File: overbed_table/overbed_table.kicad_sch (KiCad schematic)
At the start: 0 parts

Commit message: 更新原理图
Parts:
- added C33, C42, C43, C44: 1uF, PCM_SparkFun-Resistor:R_0603_1608Metric, symbol Device:C
- added CN3: KF2EDGRC-5.08-2P, lcsc_footprints:C441236_CONN-TH_P5_08_KF2EDGRC-5_08-2P, symbol lcsc_imported:KF2EDGRC-5_08-2P
- added CN4: KF2EDGRC-5.08-4P, lcsc_footprints:C441238_CONN-TH_4P-P5_08_KF2EDGRC-5_08-4P, symbol lcsc_imported:KF2EDGRC-5_08-4P
- added D7: PMEG2010ER, Diode_SMD:Nexperia_CFP3_SOD-123W, symbol Diode:PMEG2010ER
- added H1: LAIL-PZ2.54-4P-L, lcsc_footprints:C54950602_CONN-TH_LAIL-PZ2_54-4P-L, symbol lcsc_imported:LAIL-PZ2_54-4P-L
- added R34, R37, R38, R44: 10k, PCM_SparkFun-Resistor:R_0603_1608Metric, symbol PCM_SparkFun-Resistor:R
- added R35, R36: 33, PCM_SparkFun-Resistor:R_0603_1608Metric, symbol PCM_SparkFun-Resistor:R
- added SW13, SW14: KH-6X6X6H-STM, lcsc_footprints:C2837532_SW-SMD_4P-L6_0-W6_0-P4_50-LS9_0_KH-6X6X6H-STM, symbol lcsc_imported:KH-6X6X6H-STM
- added TP11: TestPoint, symbol Connector:TestPoint
- added U13, U15, U18: WAFER-XH254WZ-2A, lcsc_footprints:C7432691_CONN-TH_2P-P2_50_WAFER-XH254WZ-2A, symbol lcsc_imported:WAFER-XH254WZ-2A
- added U19: AP2112K-3.3TRG1, lcsc_footprints:C51118_SOT-25-5_L2_9-W1_6-P0_95-LS2_8-BL, symbol lcsc_imported:AP2112K-3_3TRG1
- added U6: ESP32-C3-WROOM-02, RF_Module:ESP32-C3-WROOM-02, symbol RF_Module:ESP32-C3-WROOM-02
- added X1, X2: AFA01-S05FCA-00, lcsc_footprints:C262753_FPC-SMD_AFA01-S05FCA-00, symbol lcsc_imported:AFA01-S05FCA-00
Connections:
- net 12V_5V/5V_OUT: now also X2.4
- net GND: now also C33.2, C42.2, C43.1, C44.2, CN3.1, CN4.4, H1.4, R44.2, SW13.4 (D), SW14.4 (D), U19.2 (GND), U6.19 (GND), U6.9 (GND), X2.5, X2.6, X2.7
- net 数码管_按钮/5V_IN: now also X1.4
- net 数码管_按钮/CLK: now also X1.2
- net 数码管_按钮/DIO: now also X1.3
- net 数码管_按钮/GND_IN: now also X1.5, X1.6, X1.7
- net 数码管_按钮/STB: now also X1.1
- new net: C43.2, H1.1, U19.1 (VIN), U19.3 (EN)
- new net: R35.1, U6.13 (IO18)
- new net: R36.1, U6.14 (IO19)
- new net: TP11.1, U6.6 (IO7)
- new net: C44.1, D7.2 (A), U19.5 (VOUT)
- new net +12V: CN3.2, CN4.3, U13.1, U15.1
- new net +3V3: D7.1 (K), R34.1, R37.1, R38.1, U18.1, U6.1 (3V3)
- new net 3V3_5V_转换器/3V3_SIG0: X2.3
- new net 3V3_5V_转换器/3V3_SIG1: X2.2
- new net 3V3_5V_转换器/3V3_SIG2: X2.1
- new net 3V3_5V_转换器/5V_SIG0: U6.18 (IO0)
- new net 3V3_5V_转换器/5V_SIG1: U6.17 (IO1)
- new net 3V3_5V_转换器/5V_SIG2: U6.15 (IO3)
- new net ESP32_BOOT: R37.2, SW14.2 (B), U6.8 (IO9)
- new net ESP32_D+: H1.3, R36.2
- new net ESP32_D-: H1.2, R35.2
- new net ESP32_EN: C33.1, R34.2, SW13.2 (B), U6.2 (EN)
- new net ESP32_GPIO2: R38.2, U6.16 (IO2)
- new net E_STOP: C42.1, R44.1, U18.2, U6.4 (IO5)
- new net LED1_PWM: U6.3 (IO4)
- new net LED2_PWM: U6.5 (IO6)
- new net LED灯驱动/LED_Drain: U13.2
- new net LED灯驱动1/LED_Drain: U15.2
- new net RS485_DE: U6.10 (IO10)
- new net RS485_ESP32/RS485_A: CN4.1
- new net RS485_ESP32/RS485_B: CN4.2
- new net RS485_ESP32/RS485_RX: U6.11 (IO20/RXD)
- new net RS485_ESP32/RS485_TX: U6.12 (IO21/TXD)
- no-connect marks 0 -> 5
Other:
- removed sheet 升降电机驱动
- removed sheet 步进驱动
- added sheet LED灯驱动 (LED灯驱动.kicad_sch)
- added sheet LED灯驱动1 (LED灯驱动.kicad_sch)
- added sheet RS485_ESP32 (RS485_ESP32.kicad_sch)
- added sheet 桌脚小板 (桌脚小板.kicad_sch)
- sheet 12V_3V3 ports: added GND; removed GND_IN, GND_OUT
- sheet 12V_5V ports: added GND; removed GND_IN, GND_OUT
- sheet 3V3_5V_转换器 ports: added 3V3_SIG0, 3V3_SIG1, 3V3_SIG2, 5V_SIG0, 5V_SIG1, 5V_SIG2; removed 3V3_SIG, 5V_SIG

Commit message: 更新原理图
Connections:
- net 3V3_5V_转换器/3V3_SIG0: now also U6.18 (IO0); no longer X2.3
- net 3V3_5V_转换器/3V3_SIG1: now also U6.17 (IO1); no longer X2.2
- net 3V3_5V_转换器/3V3_SIG2: now also U6.15 (IO3); no longer X2.1
- net 3V3_5V_转换器/5V_SIG0: now also X2.3; no longer U6.18 (IO0)
- net 3V3_5V_转换器/5V_SIG1: now also X2.2; no longer U6.17 (IO1)
- net 3V3_5V_转换器/5V_SIG2: now also X2.1; no longer U6.15 (IO3)
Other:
- moved on the sheet: C33, C42, C43, C44, CN3, D7, H1, R34, R37, R38, R44, SW13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

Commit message: 原理图V1.0
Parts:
- removed CN3: KF2EDGRC-5.08-2P, lcsc_footprints:C441236_CONN-TH_P5_08_KF2EDGRC-5_08-2P, symbol lcsc_imported:KF2EDGRC-5_08-2P
- removed TP11: TestPoint, symbol Connector:TestPoint
- removed U13, U15: WAFER-XH254WZ-2A, lcsc_footprints:C7432691_CONN-TH_2P-P2_50_WAFER-XH254WZ-2A, symbol lcsc_imported:WAFER-XH254WZ-2A
- added C2: 470uF, Capacitor_SMD:CP_Elec_10x10.5, symbol Device:C_Polarized
- added C5: 100nF, Capacitor_SMD:C_0603_1608Metric, symbol Device:C
- added C6: 10uF, Capacitor_SMD:C_0603_1608Metric, symbol Device:C
- added CN10, CN8, CN9: DLL-5569-2AW, lcsc_footprints:C22365654_CONN-TH_DLL-5569-2AW-GOLD-GR, symbol lcsc_imported:DLL-5569-2AW
- added CN3: KF2EDGRC-5.08-4P, lcsc_footprints:C441238_CONN-TH_4P-P5_08_KF2EDGRC-5_08-4P, symbol lcsc_imported:KF2EDGRC-5_08-4P
- added D1: SMCJ12A, PCM_Diode_SMD_AKL:D_SMC, symbol PCM_Diode_TVS_AKL:SMCJ12A
- added F1, F2, F3: 3557-2, lcsc_footprints:C352820_FUSE-TH_4P-L19_8-W6_7_3557-2, symbol lcsc_imported:3557-2
- added U4, U5, U6: BSMD2920-500-24V, lcsc_footprints:C20539727_F2920, symbol lcsc_imported:BSMD2920-500-24V
- added U7: KF7620-7.62-2P, lcsc_footprints:C475104_CONN-TH_P7_62_KF7620-7_62-2P, symbol lcsc_imported:KF7620-7_62-2P
- C1: renamed from C33; footprint PCM_SparkFun-Resistor:R_0603_1608Metric -> Capacitor_SMD:C_0603_1608Metric
- C3: renamed from C43; footprint PCM_SparkFun-Resistor:R_0603_1608Metric -> Capacitor_SMD:C_0603_1608Metric
- C4: renamed from C44; footprint PCM_SparkFun-Resistor:R_0603_1608Metric -> Capacitor_SMD:C_0603_1608Metric
- C7: renamed from C42; footprint PCM_SparkFun-Resistor:R_0603_1608Metric -> Capacitor_SMD:C_0603_1608Metric
- renumbered CN4 to CN2, D7 to D2, R34 to R1, R37 to R2, R38 to R3, R35 to R4, R36 to R5, R44 to R6, SW13 to SW1, SW14 to SW2, U19 to U1, U6 to U2, U18 to U3, X2 to X1, X1 to X2
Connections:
- net +12V: now also C2.1, D1.1 (K), F1.3, F1.4, F2.3, F2.4, F3.3, F3.4, U4.1, U5.1, U6.1; no longer CN2.3
- net +3V3: now also C5.2, C6.2
- net GND: now also C2.2, C5.1, C6.1, CN3.4, D1.2 (A), U7.1
- net LED灯驱动/LED_Drain: now also CN8.2
- net LED灯驱动1/LED_Drain: now also CN9.2
- net RS485_ESP32/RS485_A: now also CN3.1
- net RS485_ESP32/RS485_B: now also CN3.2
- net LED3_PWM: now reaches U2.6 (IO7)
- new net: CN3.3, F3.1, F3.2
- new net: CN9.1, U5.2
- new net: CN10.1, U6.2
- new net: F1.1, F1.2, U7.2
- new net: CN8.1, U4.2
- new net: CN2.3, F2.1, F2.2
- new net LED灯驱动2/LED_Drain: CN10.2
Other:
- sheet 桌脚小板 renamed 桌脚小板_1
- added sheet LED灯驱动2 (LED灯驱动.kicad_sch)
- added sheet 桌脚小板_2 (桌脚小板.kicad_sch)
- moved on the sheet: C7, CN2, R6, U3, X2

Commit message: 更新pcb
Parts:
- added R80: 10k, PCM_SparkFun-Resistor:R_0603_1608Metric, symbol PCM_SparkFun-Resistor:R
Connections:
- net +3V3: now also R80.1
- net ESP32_GPIO8: now reaches U2.7 (IO8)
- net ESP32_GPIO8: now also R80.2
- no-connect marks 5 -> 4

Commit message: update: 拆分主控板和侧板至两个文件
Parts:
- removed X2: AFA01-S05FCA-00, lcsc_footprints:C262753_FPC-SMD_AFA01-S05FCA-00, symbol lcsc_imported:AFA01-S05FCA-00
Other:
- removed sheet 数码管_按钮
- removed sheet 桌脚小板_1
- removed sheet 桌脚小板_2

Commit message: update: 添加侧板封装映射文件
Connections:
- net 12V_5V/5V_OUT renamed +5V
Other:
- note added: "BOOT相关GPIO"
- note added: "LED驱动"
- note added: "入口电路"
- note added: "急停按钮"
- note added: "烧录端口和5v转3v3 USB供电"
- moved on the sheet: C2, C3, C4, C7, D1, D2, F1, H1, R6, U1, U3, U7

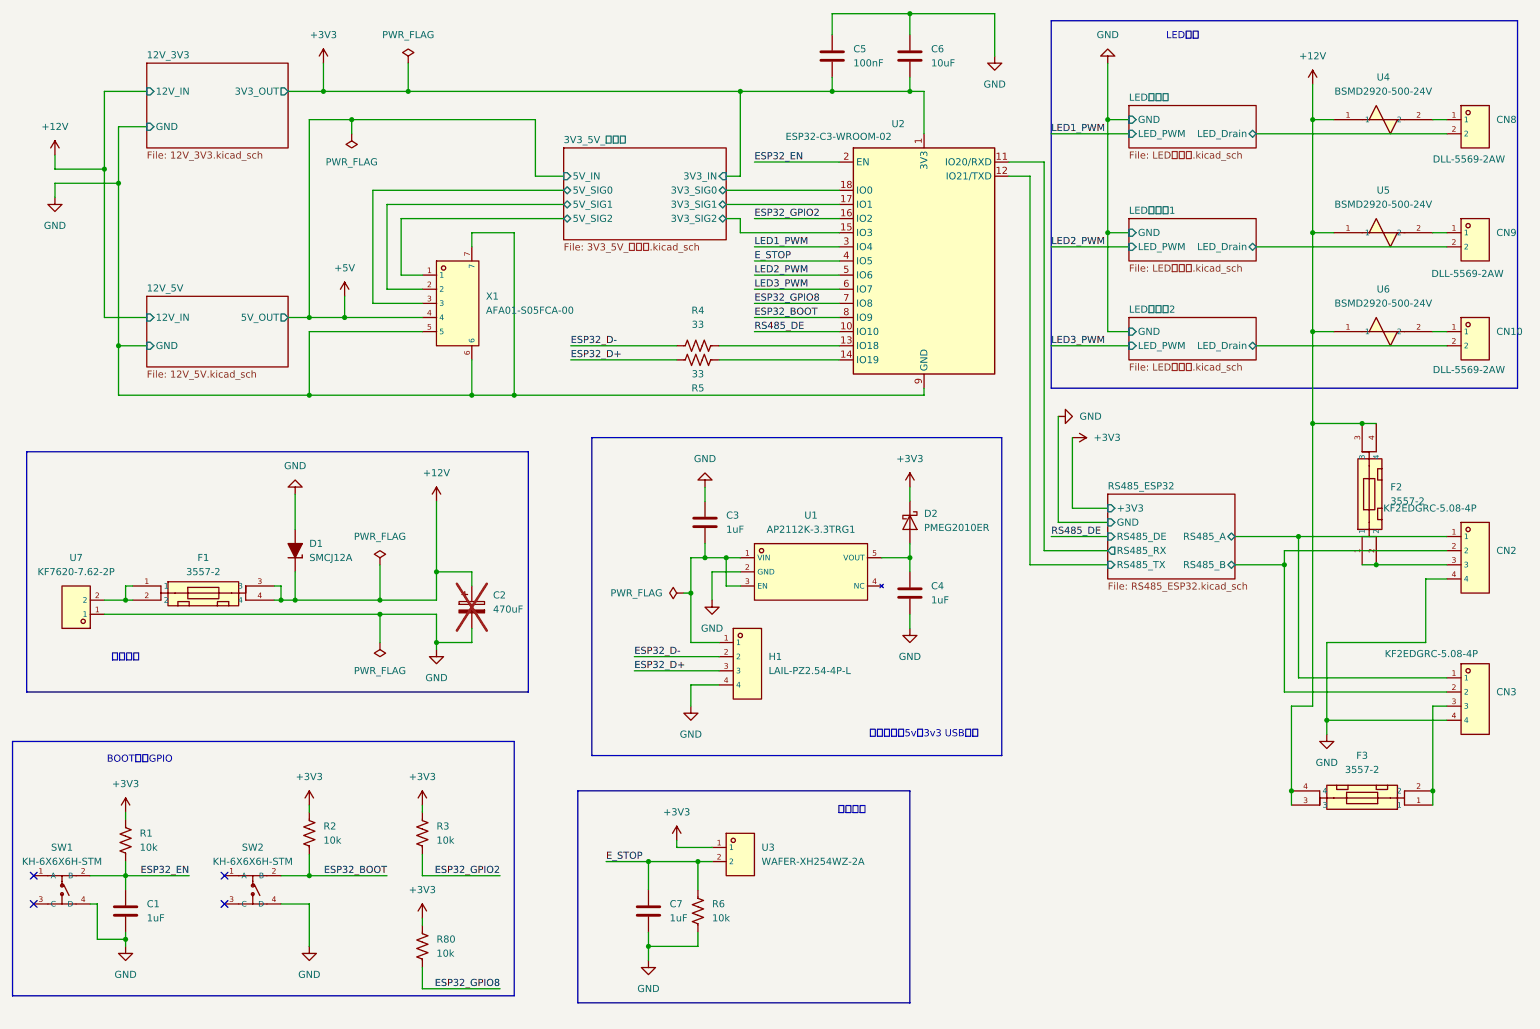
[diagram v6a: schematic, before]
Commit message: update: 更新ESP32 PCB
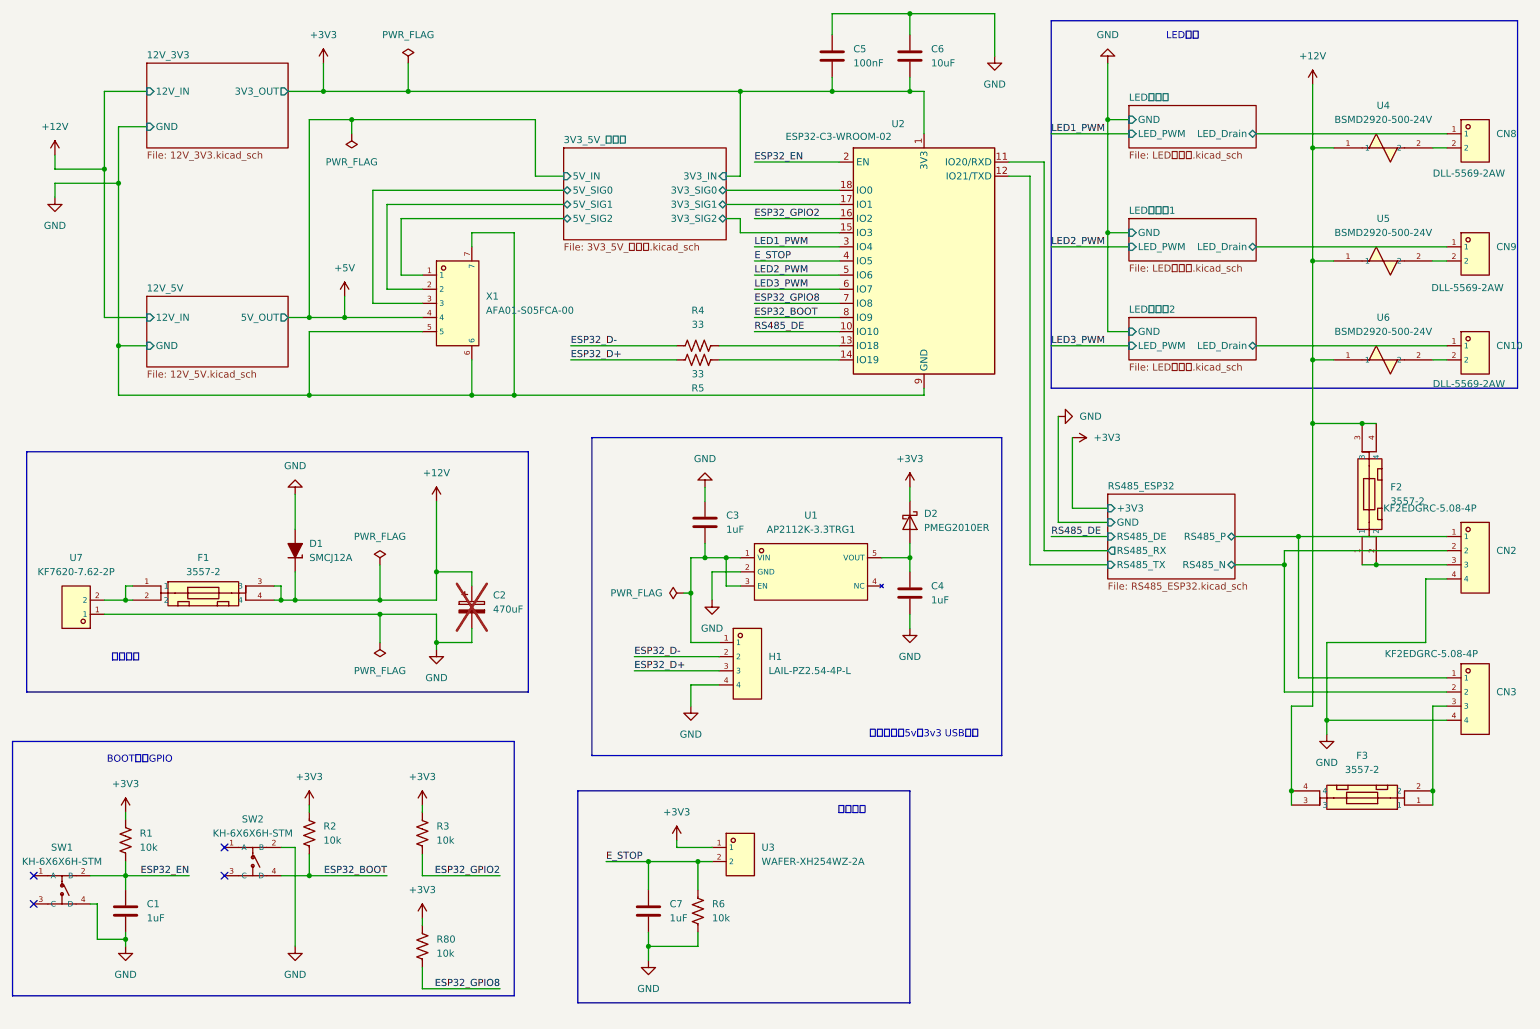
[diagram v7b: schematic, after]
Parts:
- R1, R2, R3, R4, R5, R6, R80: footprint PCM_SparkFun-Resistor:R_0603_1608Metric -> Resistor_SMD:R_0603_1608Metric
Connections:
- net ESP32_BOOT: now also SW2.4 (D); no longer SW2.2 (B)
- net GND: now also SW2.2 (B); no longer SW2.4 (D)
- net LED灯驱动/LED_Drain: now also CN8.1; no longer CN8.2
- net LED灯驱动1/LED_Drain: now also CN9.1; no longer CN9.2
- net LED灯驱动2/LED_Drain: now also CN10.1; no longer CN10.2
- net at U5.2: now also CN9.2; no longer CN9.1
- net at U6.2: now also CN10.2; no longer CN10.1
- net at U4.2: now also CN8.2; no longer CN8.1
- net RS485_ESP32/RS485_A renamed RS485_ESP32/RS485_P
- net RS485_ESP32/RS485_B renamed RS485_ESP32/RS485_N
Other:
- sheet RS485_ESP32 ports: added RS485_N, RS485_P; removed RS485_A, RS485_B
- moved on the sheet: CN10, CN8, CN9, SW2, U4, U5, U6

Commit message: update: 更新ESP32 PCB V1.0.0
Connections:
- net 3V3_5V_转换器/3V3_SIG0: now also U2.3 (IO4); no longer U2.18 (IO0)
- net 3V3_5V_转换器/3V3_SIG1: now also U2.5 (IO6); no longer U2.17 (IO1)
- net 3V3_5V_转换器/3V3_SIG2: now also U2.6 (IO7); no longer U2.15 (IO3)
- net LED1_PWM: now also U2.18 (IO0); no longer U2.3 (IO4)
- net LED2_PWM: now also U2.17 (IO1); no longer U2.5 (IO6)
- net LED3_PWM: now also U2.15 (IO3); no longer U2.6 (IO7)
